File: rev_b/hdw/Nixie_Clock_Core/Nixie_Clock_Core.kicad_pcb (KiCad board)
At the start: 4 copper layers, 200 x 50 mm, 336 parts, among them J1301 USB_B_Mini, J1901 Conn_02x32_Top_Bottom, J201 +24V IN, J2101 I2C, J2102 USB UART, J801 PICKIT4, Q2101 BSS214NW, Q401 BSS214NW, Q402 ZXMS6004FFTA, Q601 IRFL214, Q701 BSS192PH6327FTSA1, Q801 BSS214NW, SW801 MRST, U1001 PIC32MZ2048EFG100_IPF, U1101 74LVC1G97, U1201 DS3231MZ, U1202 TLV6700, U1301 TLV6700, U1302 FT234XD, U1303 74LVC1G97, U1304 ISO7321C, U1305 TPD3S014DBVR, U1401 DS1683, U1501 74LVC1G97, U1502 74LVC1G97, U1503 74LVC1G97, U1504 74LVC1G97, U1505 74LVC1G97, U1601 74LVC1G97, U1602 74LVC1G97, U1603 74LVC1G97, U1604 74LVC1G97, U1701 74VHC541, U1702 74VHC541, U1703 74VHC541, U1801 TCA9803, U1802 74VHC541, U201 TPS26600RHFT, U2101 LTC6900, U2102 74LVC1G97, U2103 MCP9804, U301 INA219BxDCN, U302 MCP9804, U401 LT8609A-DD, U501 INA219BxDCN, U502 MCP9804, U601 TLV6700, U602 LT3757, U603 TLV6700, U701 OPA333xxDCK, U702 MCP9804, U703 INA219BxDCN, U704 OPA333xxDCK, U705 OPA333xxDCK, X1101 ASE-8.000MHz, X1102 ECS-327KE

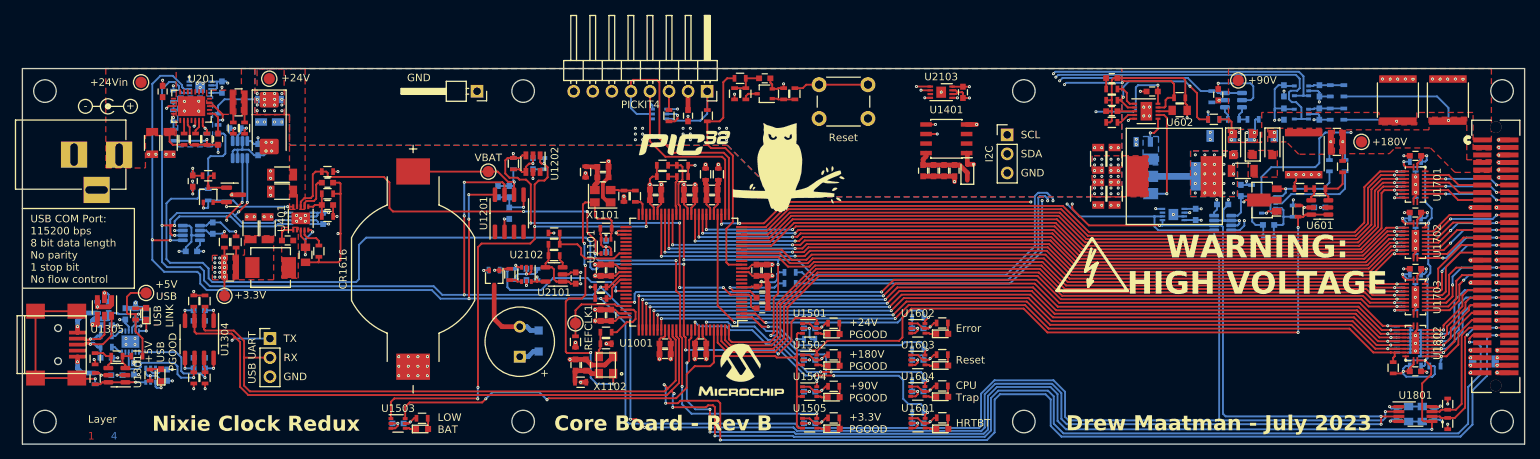
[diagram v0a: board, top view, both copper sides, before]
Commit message: fixed some core board ERC issues
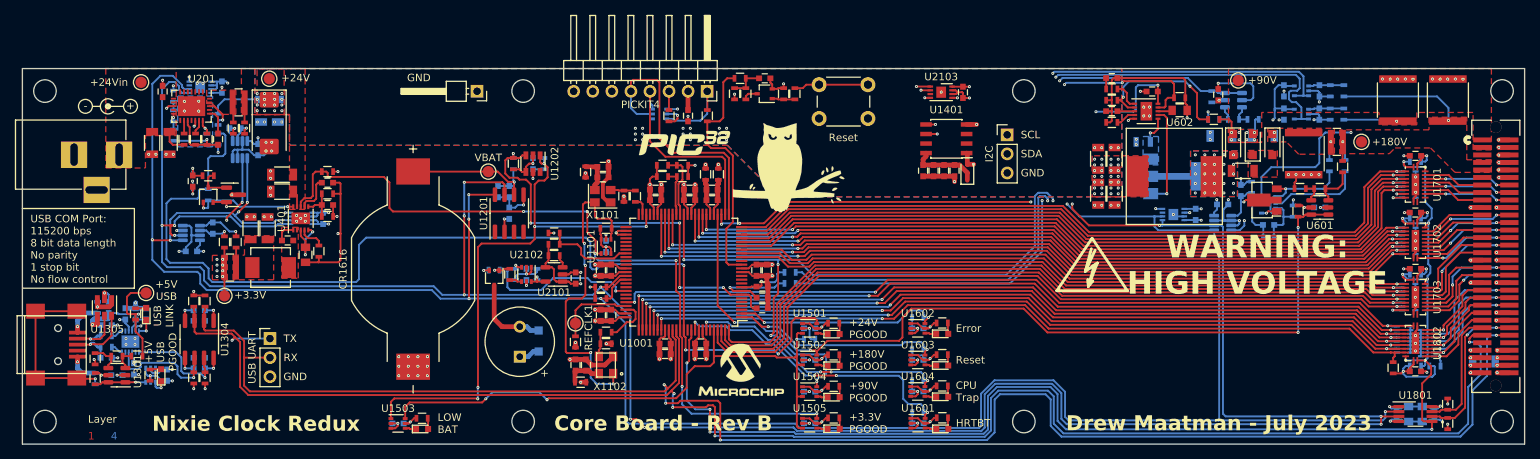
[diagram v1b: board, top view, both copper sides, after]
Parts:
- moved R702 0.46 mm to (198.7, 84.6)
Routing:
- net Net-(RN1703-R8.2): track 2.43 -> 2.94 mm
- net +3.3V: track 205.3 -> 204.9 mm, vias 75 -> 68
- net GND: track 314.2 -> 314.5 mm, vias 176 -> 175
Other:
- board text added: "TO-DO: * Custom Gold Project Logo * Layout stats * Easter egg under PIC"
- board text removed: "TO-DO: * ERC * Custom Gold Project Logo * Layout stats * Easter egg under PIC"

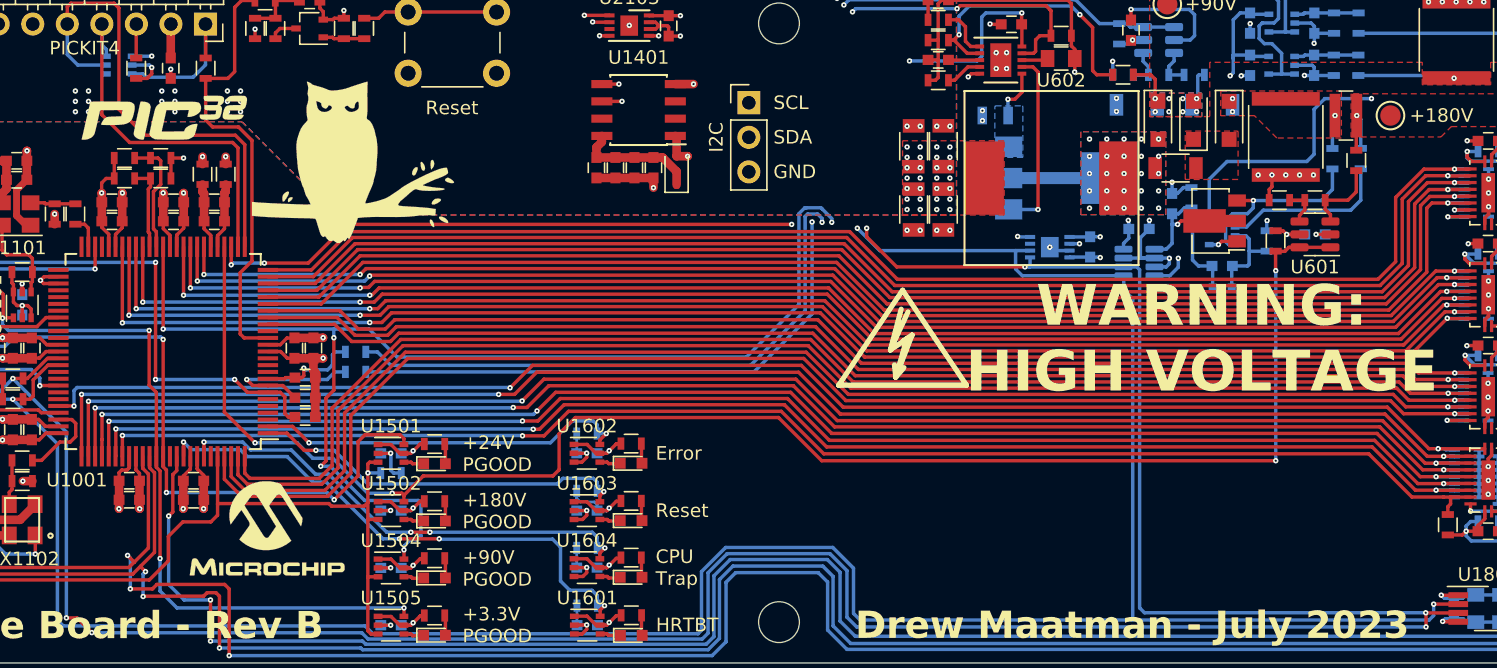
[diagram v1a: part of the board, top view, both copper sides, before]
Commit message: added BOM
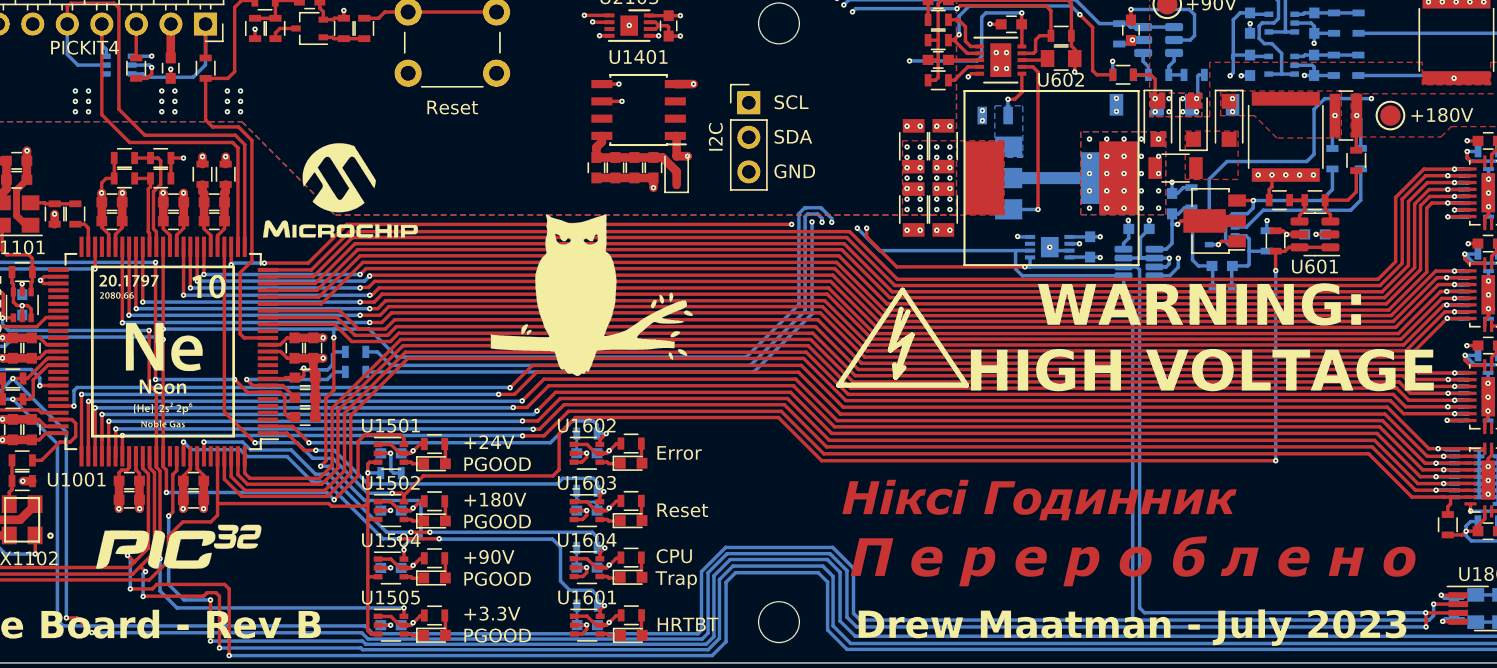
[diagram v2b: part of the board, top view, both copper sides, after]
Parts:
- added G***: LOGO, LOGO, F.Cu at (194.6, 109.2)
- added G***: LOGO, LOGO, F.Cu at (123.1, 95.9)
- moved G*** 31.6 mm to (124.2, 110.2)
- moved G*** 25.4 mm to (136.1, 84.0)
- moved G*** 20.1 mm to (155.0, 91.7)
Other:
- board text added: "TO-DO: * Custom Gold Project Logo * Layout stats"
- board text removed: "TO-DO: * Custom Gold Project Logo * Layout stats * Easter egg under PIC"

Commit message: generated gerbers
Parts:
- moved REF** 1.63 mm to (209.6, 98.9)
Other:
- board text added: "Nixie Clock Redux Core Board Rev B: Pads: 1228 Vias: 618 Track Segments: 2898 Nets: 264 Components: 338"
- board text removed: "TO-DO: * Custom Gold Project Logo * Layout stats"
